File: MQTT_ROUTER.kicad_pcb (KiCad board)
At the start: 2 copper layers, 85 x 100 mm, 87 parts, among them J1 Conn_2Rows-07Pins, J2 Conn_02x07_Odd_Even, J3 Screw_Terminal_01x02, J4 Screw_Terminal_01x03, J5 Screw_Terminal_01x03, J6 Screw_Terminal_01x04, J7 Screw_Terminal_01x06, K1 SANYOU_SRD_Form_C, K2 SANYOU_SRD_Form_C, Q1 SS8050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

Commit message: Actualizar PCB (2)
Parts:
- moved J1 0.07 mm to (117.3, 117.0)
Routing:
- net /CFG_MODE: track 48.0 -> 43.5 mm
- net /MTMS: track 17.6 -> 14.2 mm
- net /MTDO: track 43.6 -> 44.7 mm
- net /MTDI: track 20.2 -> 19.3 mm
- net GND: track 3.70 -> 3.64 mm, vias 72 -> 82
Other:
- board text added: "+"
- board text added: "+3"
- board text added: "+5"
- board text added: "-"
- board text added: "24V AC/DC"
- board text added: "A+"
- board text added: "B-"
- board text added: "BIAS+"
- board text added: "BIAS-"
- board text added: "C2"
- board text added: "CAN BUS"
- board text added: "CK"
- board text added: "DI"
- board text added: "DO"
- board text added: "E/S"
- board text added: "EOL"
- board text added: "G"
- board text added: "H"
- board text added: "JTAG"
- board text added: "L"
- board text added: "L1"
- board text added: "L2"
- board text added: "MODE"
- board text added: "MS"
- board text added: "N1"
- board text added: "N2"
- board text added: "NC2"
- board text added: "NO2"
- board text added: "OPTO1"
- board text added: "OPTO2"
- board text added: "POWER"
- board text added: "RS-485"
- board text added: "RS_H"
- board text added: "SCL_H"
- board text added: "SCL_L"
- board text added: "SDA_H"
- board text added: "SDA_L"
- board text added: "SS_H"
- board text added: "VN"
- board text added: "VP"

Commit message: Actualizar PCB (3)
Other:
- board text added: "MQTT ROUTER V 1.0"
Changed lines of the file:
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@@
+		)
+	)
+	(gr_text "MQTT ROUTER\nV 1.0"
+		(at 158.775 100 0)
+		(layer "F.SilkS")
+		(effects
+			(font
+				(size 1 1)
+				(thickness 0.15)
+			)
 		)
 	)

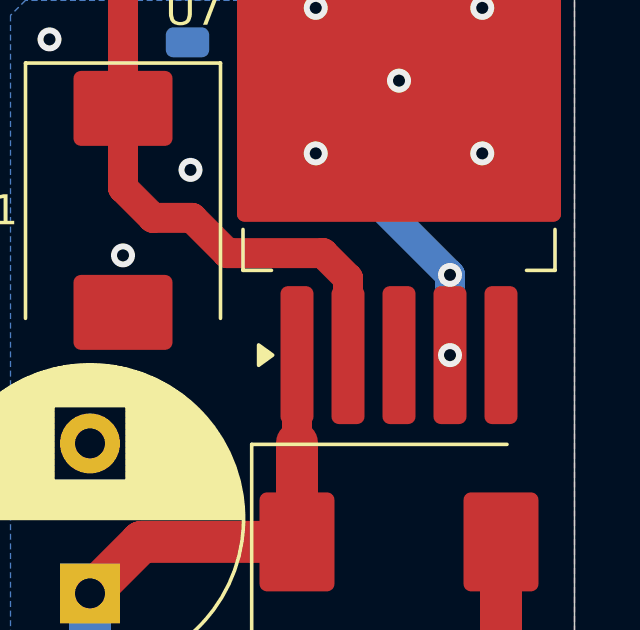
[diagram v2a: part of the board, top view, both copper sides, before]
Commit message: Aumentar distancia entre soldermask y pad en PCB
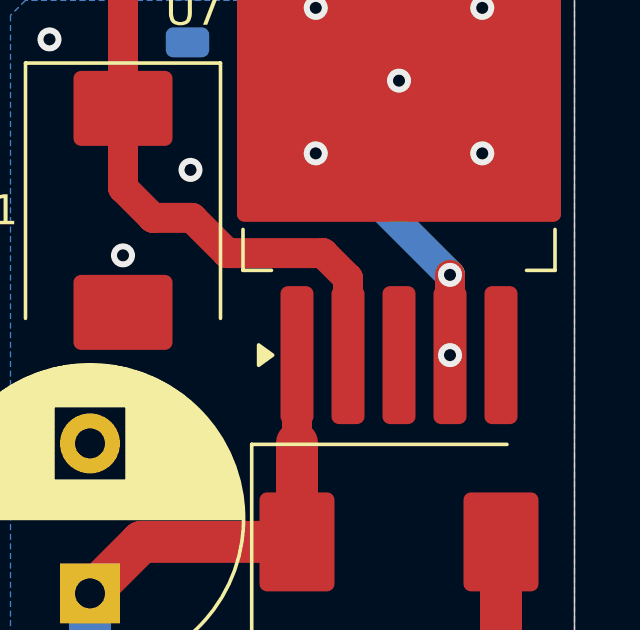
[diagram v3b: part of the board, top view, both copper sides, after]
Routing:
- net +5V: track 269.2 -> 271.8 mm
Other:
- rule pad_to_mask_clearance: 0.038 -> 0.15
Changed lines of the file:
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@@
 			(dielectric_constraints no)
 		)
-		(pad_to_mask_clearance 0.038)
+		(pad_to_mask_clearance 0.15)
 		(solder_mask_min_width 0.1)
-		(allow_soldermask_bridges_in_footprints no)
+		(allow_soldermask_bridges_in_footprints yes)
 		(pcbplotparams
 			(layerselection 0x00010fc_ffffffff)
@@
 	)
 	(segment
+		(start 179.35 106.35)
+		(end 179.35 109.025)
+		(width 1)
+		(layer "F.Cu")
+		(net 3)
+	)
+	(segment
 		(start 125.7 121.7)
 		(end 123.2 121.7)
@@
 	)
 	(segment
+		(start 179.35 106.35)
+		(end 179.35 109.025)
+		(width 1)
+		(layer "B.Cu")
+		(net 3)
+	)
+	(segment
 		(start 144.9 119.85)
 		(end 143.1 119.85)
@@
 		(width 1)
 		(layer "B.Cu")
-		(net 3)
-	)
-	(segment
-		(start 179.35 106.35)
-		(end 179.35 109.025)
-		(width 1)
-		(layer "B.Cu")

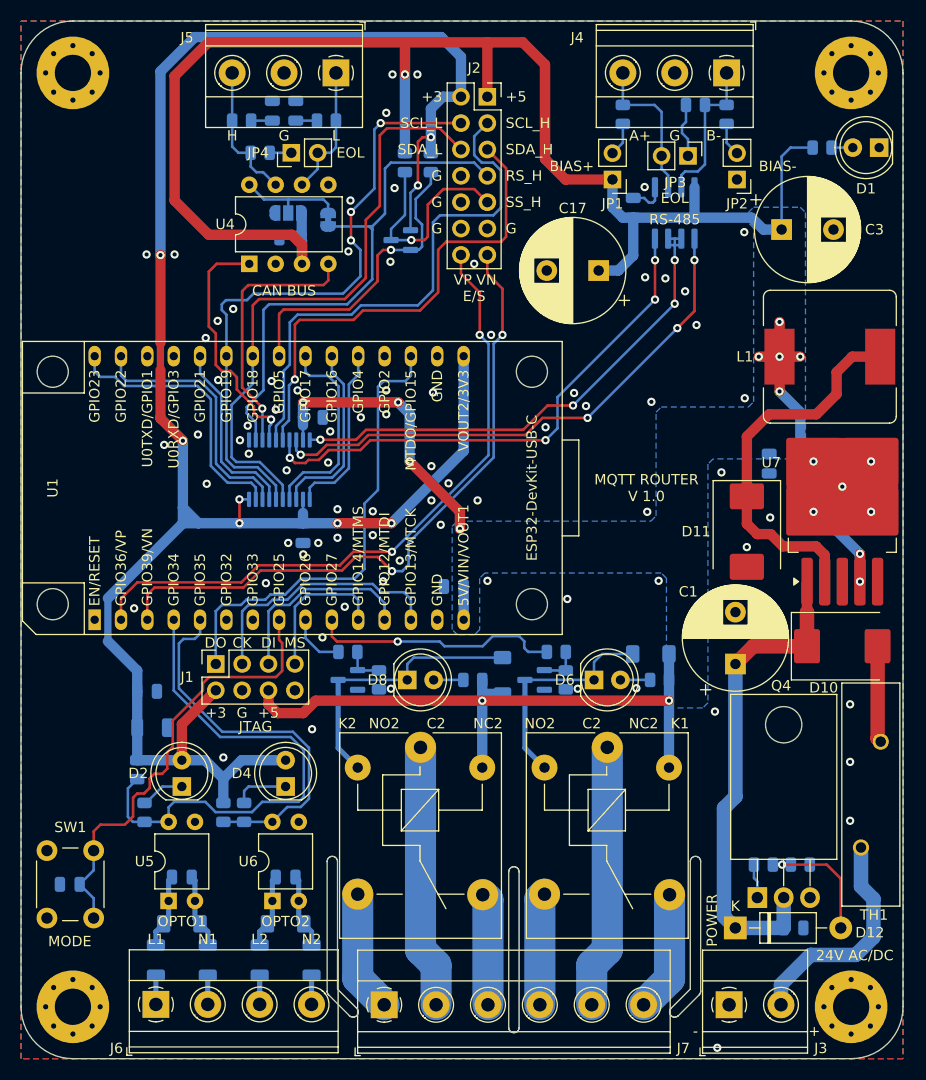
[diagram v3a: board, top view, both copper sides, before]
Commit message: Corregir distancia entre soldermask y pad en PCB
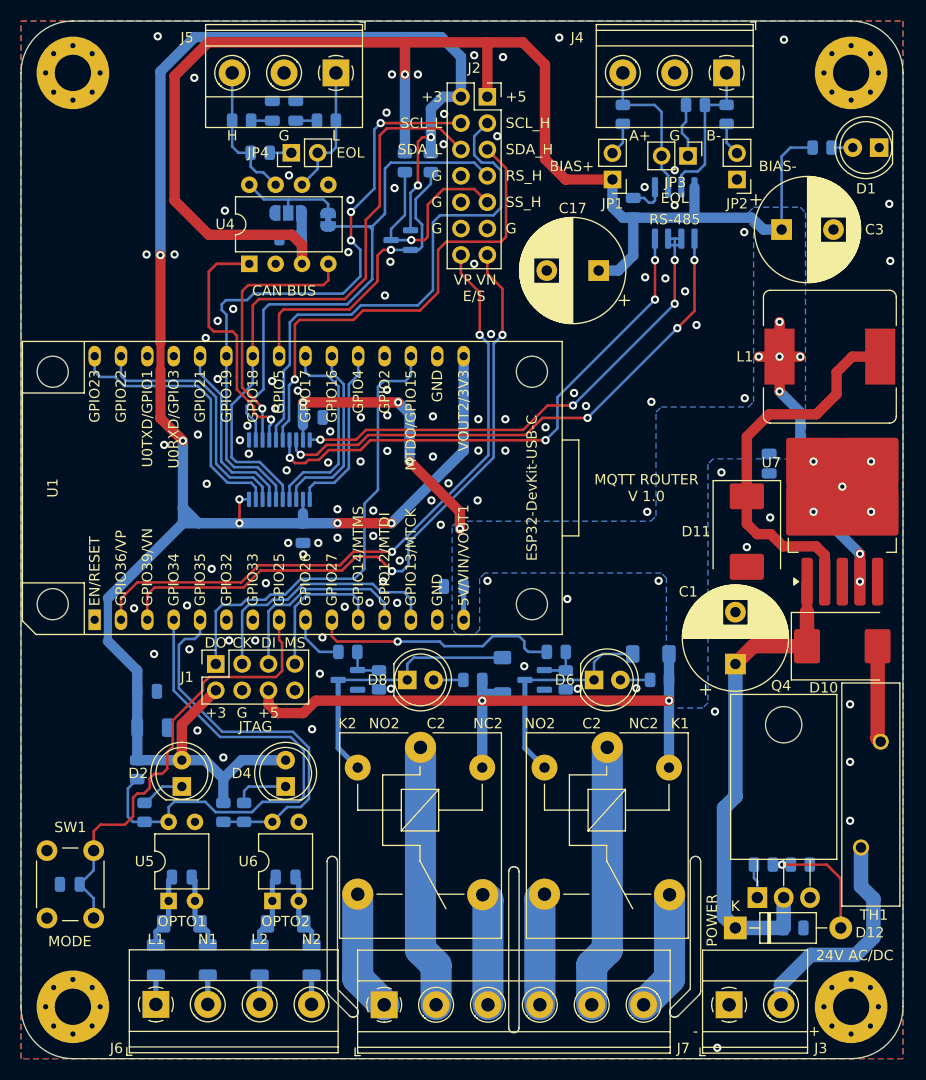
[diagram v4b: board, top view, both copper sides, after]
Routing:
- net /TXD_HI: track 24.1 -> 24.7 mm
- net GND: vias 82 -> 115
